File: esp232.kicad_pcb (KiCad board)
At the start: 2 copper layers, 35 x 40 mm, 18 parts, among them J1 RS232-Connector, J2 External-PWR, J3 Spare IO, U1 MOUDLE-SEEEDUINO-XIAO-ESP32C3, U2 MAX3232

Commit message: small layout improvements
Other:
- board text added: "+5V"
- board text added: "3V3"
- board text added: "A10"
- board text added: "A11"
- board text added: "A2"
- board text added: "A7"
- board text added: "A8"
- board text added: "A9"
- board text added: "ESP232"
- board text added: "GND"
- board text added: "USR"

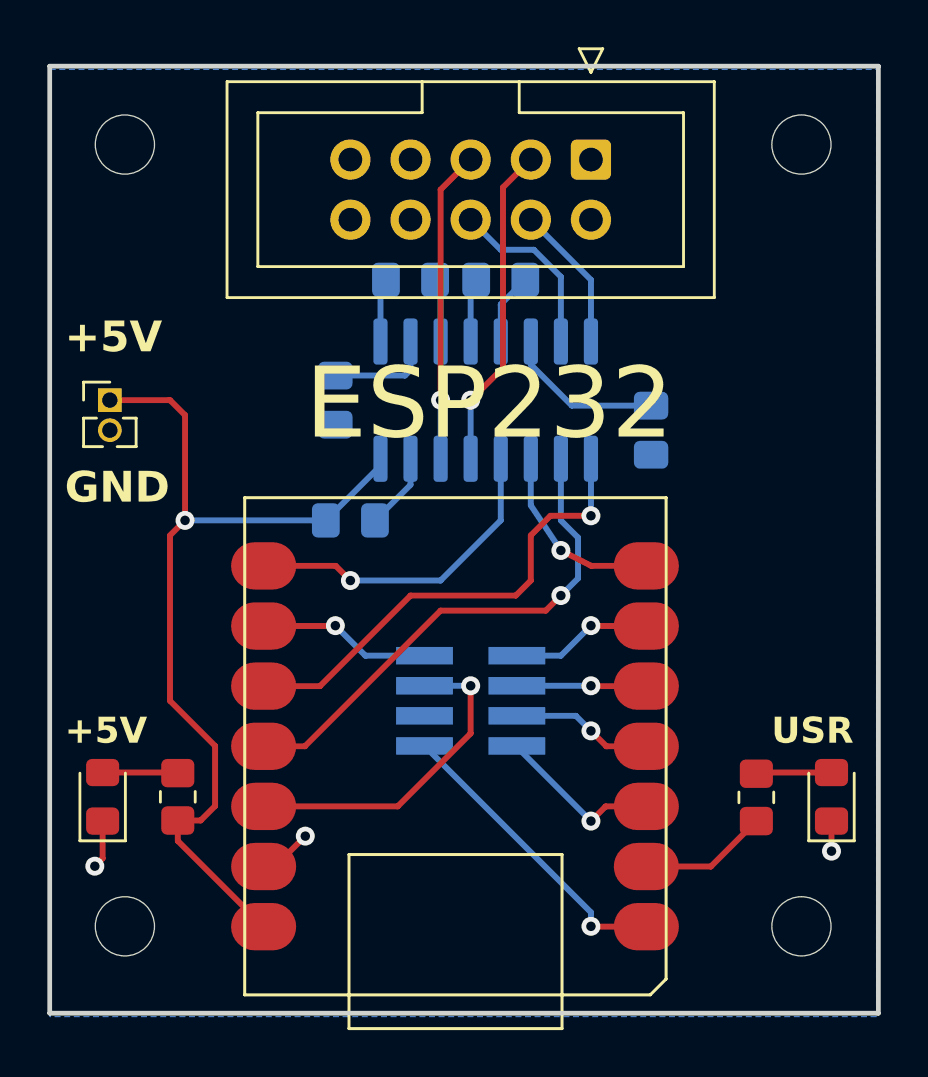
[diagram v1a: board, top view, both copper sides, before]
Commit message: fixed review comments
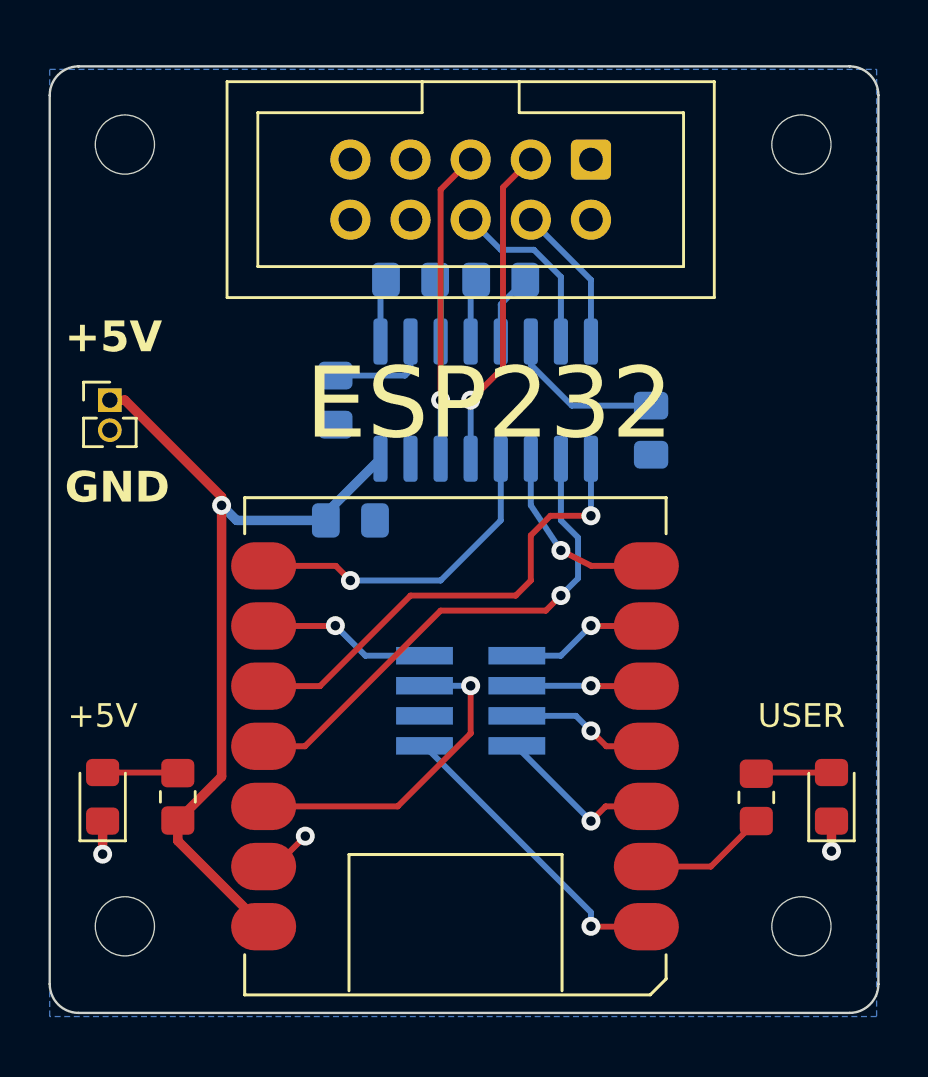
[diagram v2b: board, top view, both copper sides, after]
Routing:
- net GND: track 8.83 -> 4.96 mm
- net +5V: track 39.0 -> 36.0 mm
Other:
- outline, holes or cut-outs redrawn
- board text removed: "USR"
